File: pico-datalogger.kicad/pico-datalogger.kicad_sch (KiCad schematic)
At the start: 28 parts, among them J1 JST-PH2 VCC, J10 Conn_Inky_SW, J2 Conn_I2C_Internal, J3 RFM9x_Lora_Breakout, J4 Alt-VCC, J5 Conn_I2S, J6 Conn_Inky_SPI, J7 Micro_SD_TF_PUSH, J8 Conn_ADC, J9 Conn_UART, SW1 SW_Push_SLIM, SW2 SW_Reset, U1 SN74HC74N, U2 PCF8523T, U3 Pico, Y1 Crystal

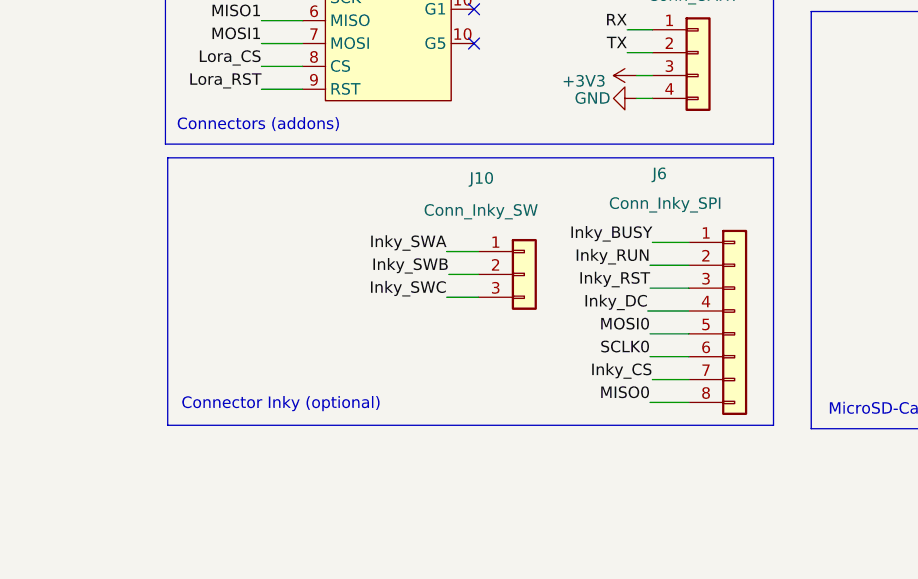
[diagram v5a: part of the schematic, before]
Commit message: fix: added 3V3 and GND for InkyPack-connector
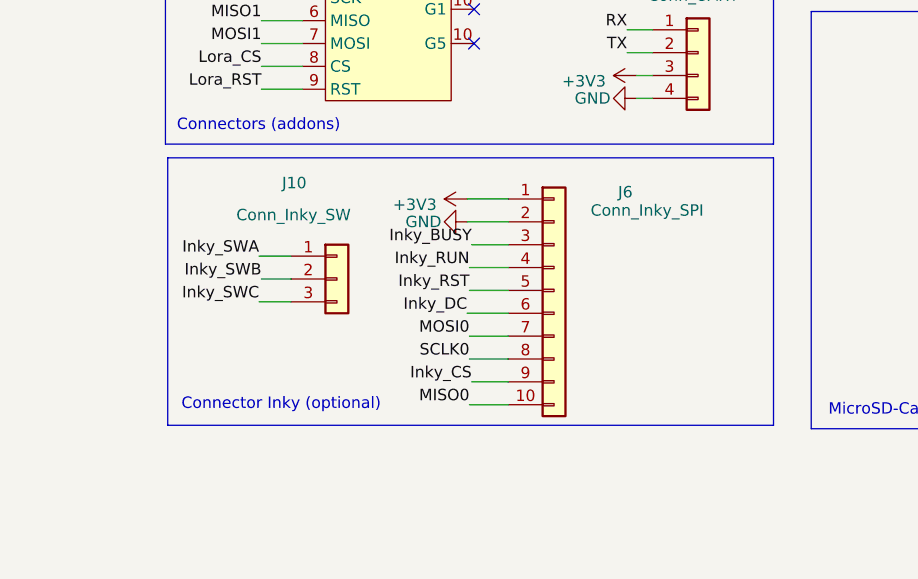
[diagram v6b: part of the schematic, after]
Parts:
- J6: footprint Connector_PinHeader_2.54mm:PinHeader_1x08_P2.54mm_Vertical -> Connector_PinHeader_2.54mm:PinHeader_1x10_P2.54mm_Vertical; symbol Connector_Generic:Conn_01x08 -> Connector_Generic:Conn_01x10
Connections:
- net +3V3: now also J6.1 (Pin_1)
- net GND: now also J6.2 (Pin_2)
- net Inky_BUSY: now also J6.3 (Pin_3); no longer J6.1 (Pin_1)
- net Inky_CS: now also J6.9 (Pin_9); no longer J6.7 (Pin_7)
- net Inky_DC: now also J6.6 (Pin_6); no longer J6.4 (Pin_4)
- net Inky_RST: now also J6.5 (Pin_5); no longer J6.3 (Pin_3)
- net Inky_RUN: now also J6.4 (Pin_4); no longer J6.2 (Pin_2)
- net MISO0: now also J6.10 (Pin_10); no longer J6.8 (Pin_8)
- net MOSI0: now also J6.7 (Pin_7); no longer J6.5 (Pin_5)
- net SCLK0: now also J6.8 (Pin_8); no longer J6.6 (Pin_6)
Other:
- moved on the sheet: J10

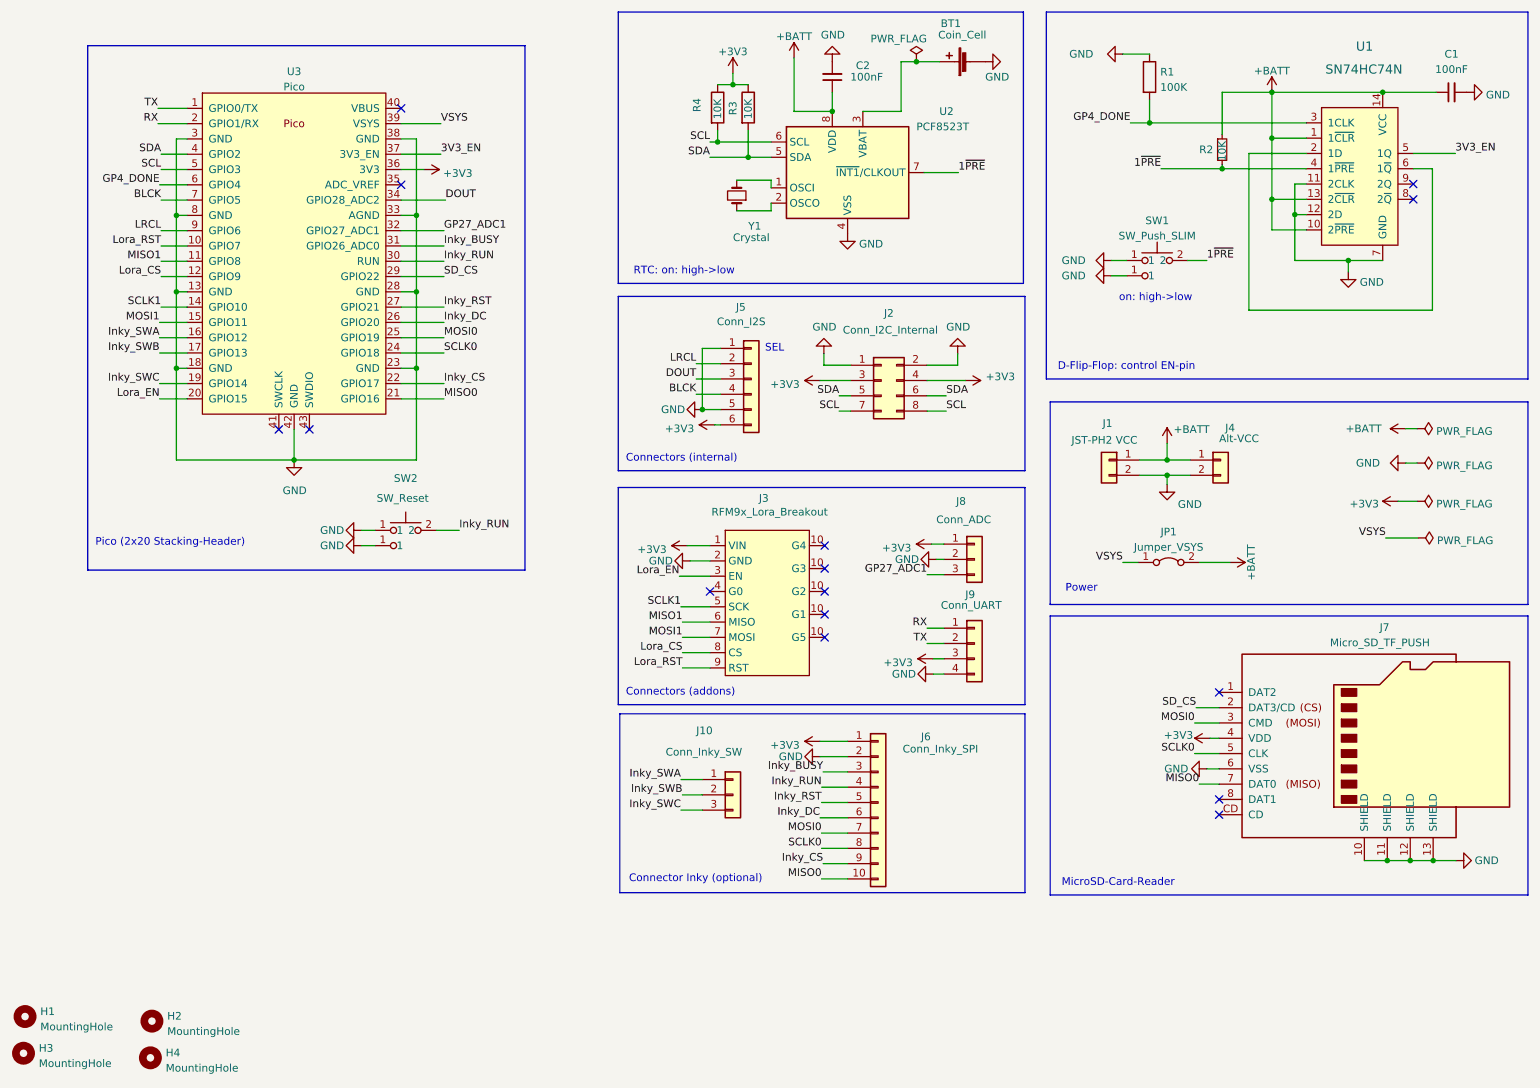
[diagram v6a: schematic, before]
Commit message: added I2C/BG connectors
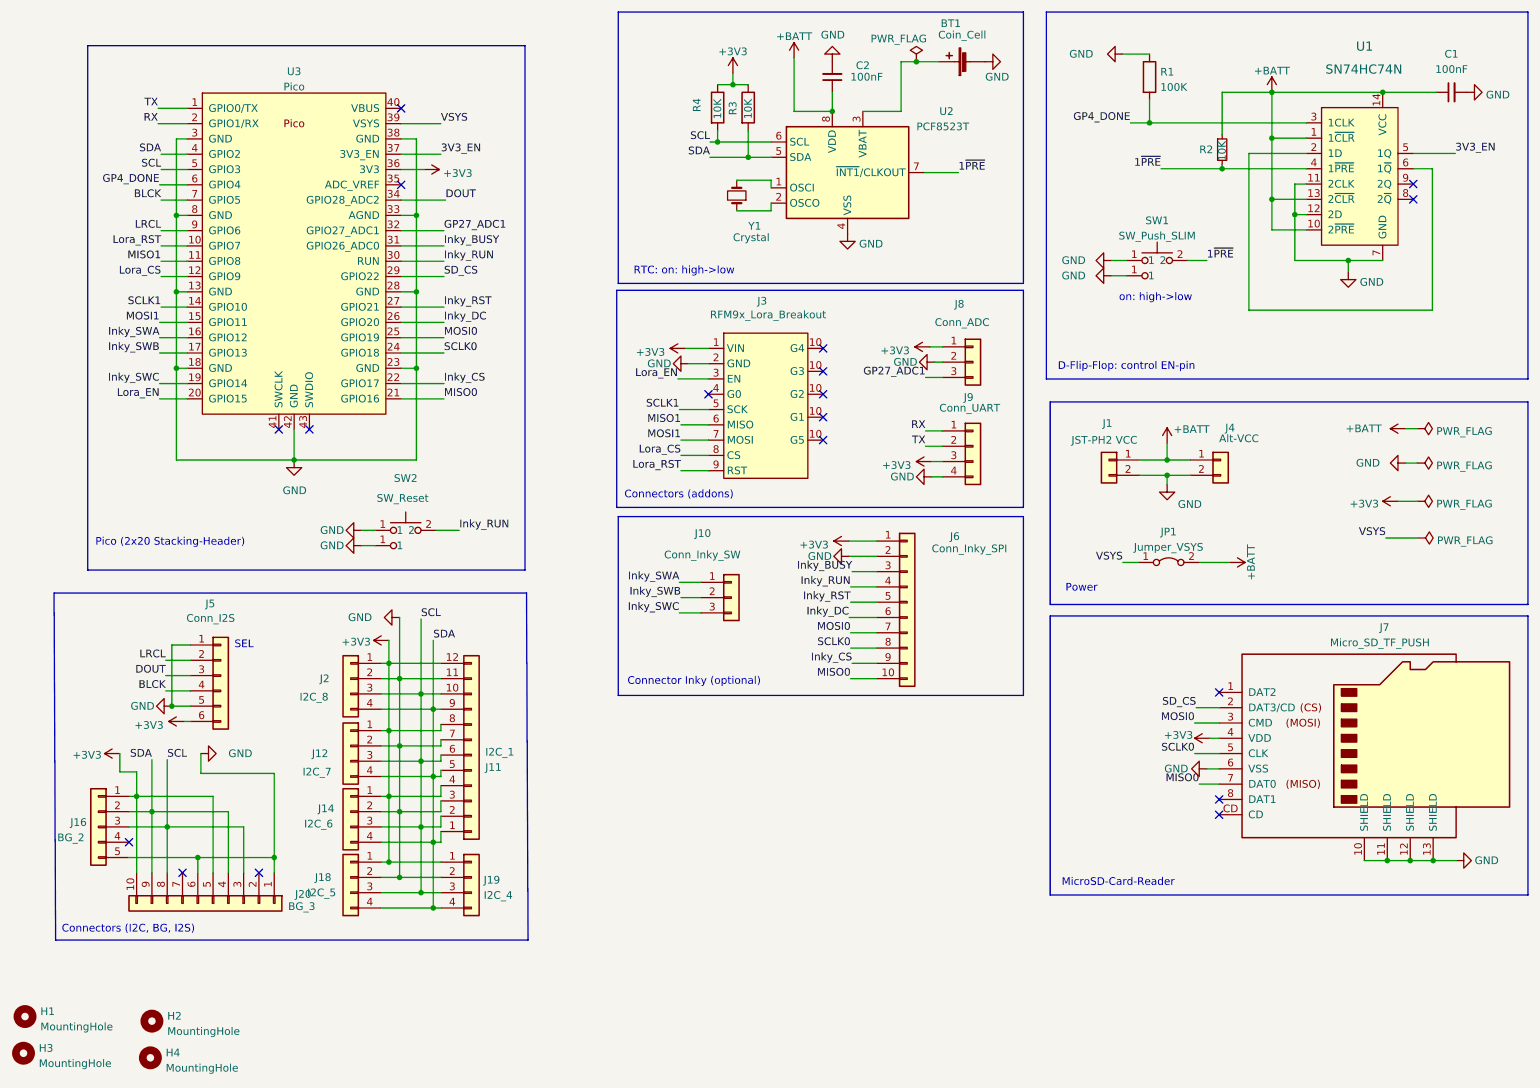
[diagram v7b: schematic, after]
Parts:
- removed J2: Conn_I2C_Internal, Connector_PinHeader_2.54mm:PinHeader_2x04_P2.54mm_Vertical, symbol Connector_Generic:Conn_02x04_Odd_Even
- added J11: I2C_1, Connector_PinHeader_2.54mm:PinHeader_1x12_P2.54mm_Horizontal, symbol Connector_Generic:Conn_01x12
- added J12: I2C_7, Connector_JST:JST_SH_SM04B-SRSS-TB_1x04-1MP_P1.00mm_Horizontal, symbol Connector_Generic:Conn_01x04
- added J14: I2C_6, Connector_JST:JST_SH_SM04B-SRSS-TB_1x04-1MP_P1.00mm_Horizontal, symbol Connector_Generic:Conn_01x04
- added J16: BG_2, Connector_PinHeader_2.54mm:PinHeader_1x05_P2.54mm_Vertical, symbol Connector_Generic:Conn_01x05
- added J18: I2C_5, Connector_JST:JST_SH_BM04B-SRSS-TB_1x04-1MP_P1.00mm_Vertical, symbol Connector_Generic:Conn_01x04
- added J19: I2C_4, Connector_PinHeader_2.54mm:PinHeader_1x04_P2.54mm_Vertical, symbol Connector_Generic:Conn_01x04
- added J2: I2C_8, Connector_JST:JST_SH_SM04B-SRSS-TB_1x04-1MP_P1.00mm_Horizontal, symbol Connector_Generic:Conn_01x04
- added J20: BG_3, Connector_PinHeader_2.54mm:PinHeader_1x10_P2.54mm_Horizontal, symbol Connector_Generic:Conn_01x10
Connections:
- net +3V3: now also J11.12 (Pin_12), J11.4 (Pin_4), J11.8 (Pin_8), J12.1 (Pin_1), J14.1 (Pin_1), J16.1 (Pin_1), J18.1 (Pin_1), J19.1 (Pin_1), J2.1 (Pin_1), J20.10 (Pin_10), J20.5 (Pin_5)
- net GND: now also J11.11 (Pin_11), J11.3 (Pin_3), J11.7 (Pin_7), J12.2 (Pin_2), J14.2 (Pin_2), J16.5 (Pin_5), J18.2 (Pin_2), J19.2 (Pin_2), J2.2 (Pin_2), J20.1 (Pin_1), J20.6 (Pin_6)
- net SCL: now also J11.10 (Pin_10), J11.2 (Pin_2), J11.6 (Pin_6), J12.3 (Pin_3), J14.3 (Pin_3), J16.3 (Pin_3), J18.3 (Pin_3), J19.3 (Pin_3), J2.3 (Pin_3), J20.3 (Pin_3), J20.8 (Pin_8)
- net SDA: now also J11.1 (Pin_1), J11.5 (Pin_5), J11.9 (Pin_9), J12.4 (Pin_4), J14.4 (Pin_4), J16.2 (Pin_2), J18.4 (Pin_4), J19.4 (Pin_4), J2.4 (Pin_4), J20.4 (Pin_4), J20.9 (Pin_9)
- no-connect marks 15 -> 18
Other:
- note added: "Connectors (I2C, BG, I2S)"
- note removed: "Connectors (internal)"
- moved on the sheet: J10, J3, J5, J6, J8, J9

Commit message: Rev 0.98: ready for production
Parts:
- H1, H2, H3, H4, J3, J8, J9, JP1, SW2: now left out of the parts list
